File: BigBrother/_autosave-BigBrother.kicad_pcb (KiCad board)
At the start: 2 copper layers, 67 x 71 mm, 4 parts, among them J1 RPi_GPIO, U1 bno055, U2 BMP388, U3 VHN5019_Breakout

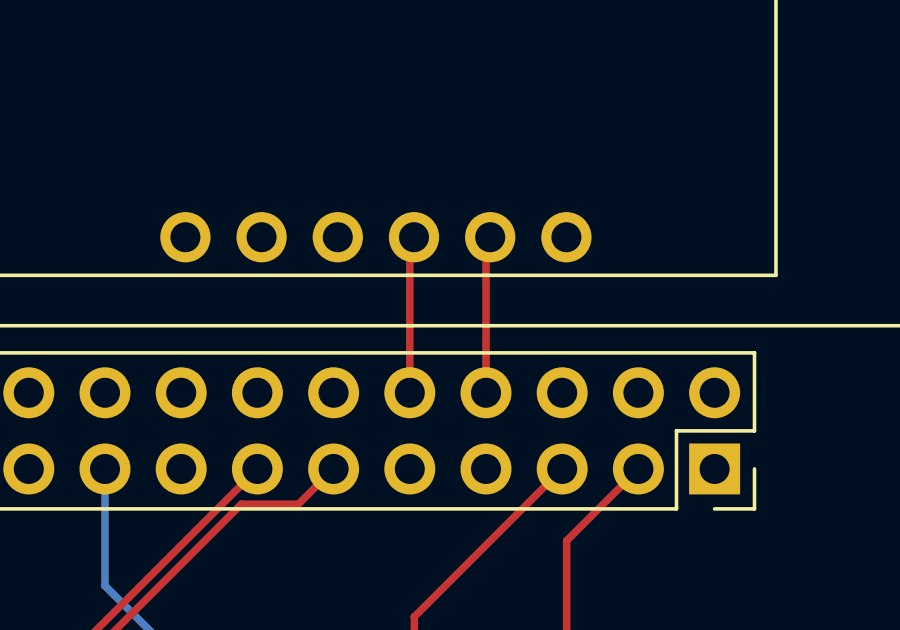
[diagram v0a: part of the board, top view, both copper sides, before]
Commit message: I forgot RST
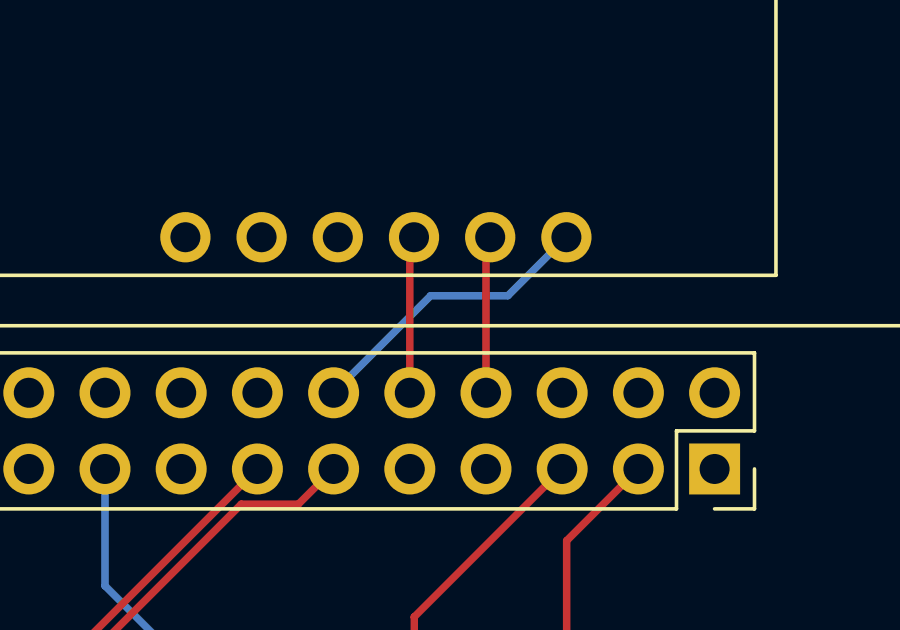
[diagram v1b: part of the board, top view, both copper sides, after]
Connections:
- J1 pad 12: Net-(J1-Pad12) -> RST
- U1 pad 6: Net-(U1-Pad6) -> RST
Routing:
- net RST: track 0.00 -> 9.91 mm
